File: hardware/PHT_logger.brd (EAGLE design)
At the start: 75 x 45 mm, 14 parts, among them IC3 ESP32-S3-WROOM-1-N16R2

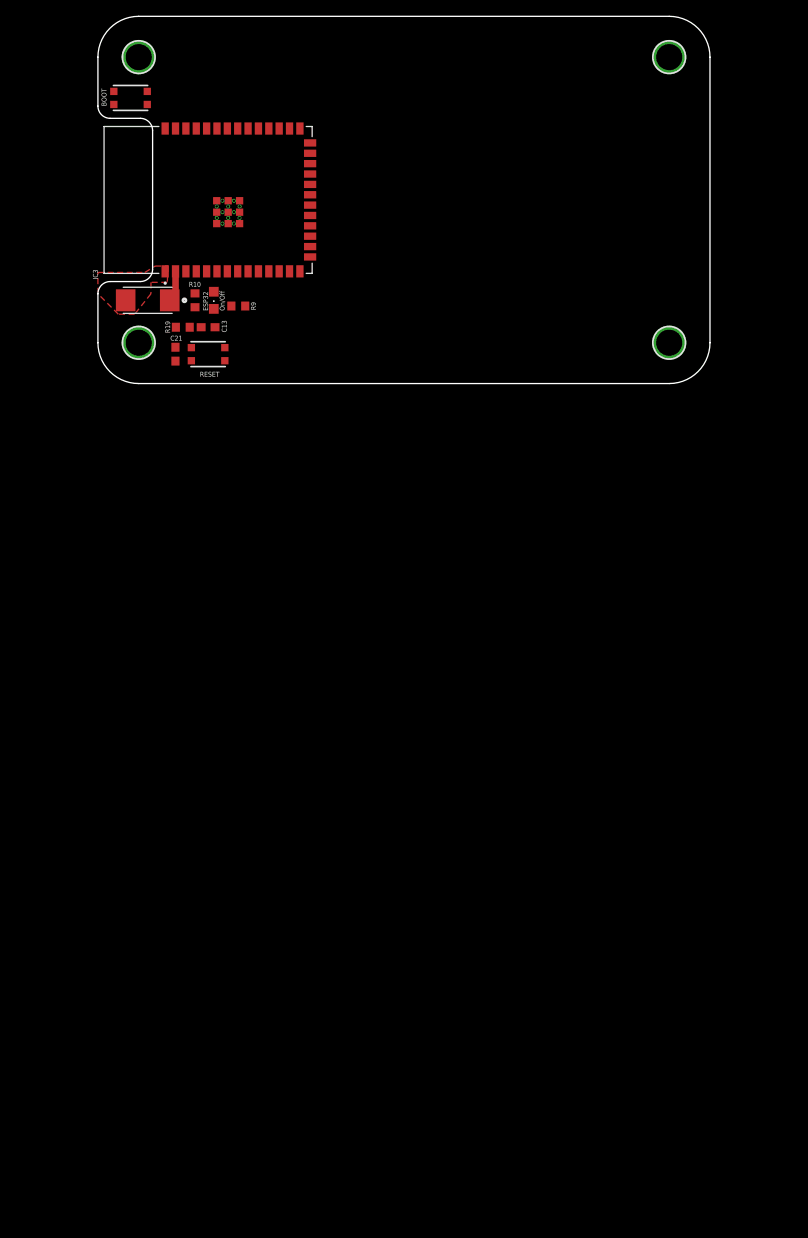
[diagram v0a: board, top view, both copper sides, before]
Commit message: Powe components updated on schematics
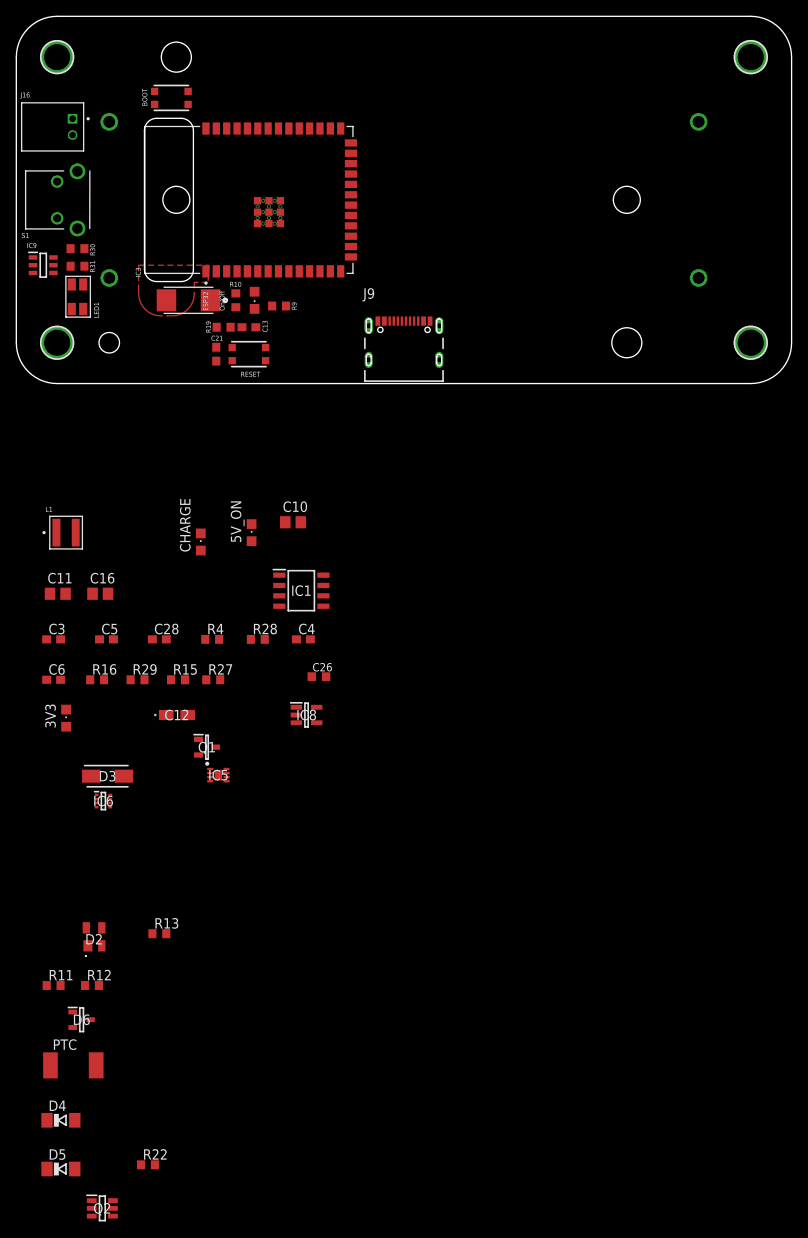
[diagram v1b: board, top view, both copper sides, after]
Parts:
- added 3V3: Red, led:CHIPLED_0805
- added 5V_ON: Yellow, led:CHIPLED_0805
- added BT1: 1049, 1049:BAT_1049
- added C10: 4.7uF, rcl:C0805
- added C11: 10uF, rcl:C0805
- added C12: T491A226M006AT7280, T491A226M006AT7280:T491A
- added C16: 22uF, rcl:C0805
- added C26: 10µF, rcl:C0603K
- added C28, C3, C5: 100nF, rcl:C0603
- added C4, C6: 10uF, rcl:C0603
- added CHARGE: Orange, led:CHIPLED_0805
- added D2: SP0503BAHTG, SP0503BAHTG:SP0503BAHTG
- added D3: RBR5L40ADDTE25, RBR5L40ADDTE25:DIOM5026X220N
- added D4, D5: bzv55-b5v6, diode:SOD80C
- added D6: BAT54,215, BAT54_215:SOT95P230X110-3N
- added IC1: AP2112M, AP2112M-3.3TRG1:SOIC127P600X170-8N
- added IC5: MAX17048G, MAX17048G+T10:SON50P200X200X80-9N
- added IC6: TPS610333DRLR, TPS610333DRLR:SOTFL50P160X60-8N
- added IC8: MCP73831T, MCP73831T-2ACI_OT:SOT95P270X145-5N
- added IC9: MAX16054AZT+T, MAX16054AZT+T:SOT95P275X110-6N
- added J16: S2B-PH, S2B-PH-K-S_LF__SN_:JST_S2B-PH-K-S(LF)(SN)
- added J9: USB4105-GF-A, USB4105-GF-A:GCT_USB4105-GF-A
- added L1: XFL4020-472MEC, XFL4020-472MEC:IND_XFL4020-472MEC
- added LED1: PWR_ON_OFF, OSRG1206C1C:3216(1206)-4
- added PTC: 1.5A, rcl:R2512
- added Q1: DMP2045U, DMP2045U-7:SOT96P240X110-3N
- added Q2: DMN2004DMK-7, DMN2004DMK-7:SOT95P285X145-6N
- added R11, R12: 5.1k, rcl:R0603
- added R13: 100k, rcl:R0603
- added R15, R22, R27, R30, R31: 1K, rcl:R0603
- added R16, R29: 5.1K, rcl:R0603
- added R28, R4: 100K, rcl:R0603
- added S1: 1-1825027-4, 1-1825027-4:118250274
- moved U$1 10.0 mm to (42.5, -17.5)
- moved U$2 10.0 mm to (-42.5, -17.5)
- moved U$3 10.0 mm to (-42.5, 17.5)
- moved U$4 10.0 mm to (42.5, 17.5)
- moved BOOT 5.00 mm to (-28.5, 12.5)
- moved C13 5.00 mm to (-19.0, -15.6)
- moved C15 5.00 mm to (-26.4, -12.3)
- moved C21 5.00 mm to (-23.0, -18.9)
- moved ESP32_ON 5.00 mm to (-18.3, -12.3)
- moved IC3 5.00 mm to (-19.0, 0.00)
- moved R10 5.00 mm to (-20.6, -12.3)
- moved R19 5.00 mm to (-22.1, -15.6)
- moved R9 5.00 mm to (-15.3, -13.0)
- moved RESET 5.00 mm to (-19.0, -18.9)
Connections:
- new net +5V: C11.2, C16.2, IC6.8, R15.1
- new net EXT_GND: D5.A, J9.S1, J9.S2, J9.S3, J9.S4, Q2.3, R13.2
- new net GATE_PROT: D4.A, Q2.5, R22.1
- new net LDO_EN: IC9.5, LED1.3, R28.1
- new net N$1: BT1.P2
- new net N$10: 5V_ON.A, R15.2
- new net N$11: CHARGE.C, R16.1
- new net N$12: IC9.4, LED1.1
- new net N$13: IC1.5, R28.2
- new net N$14: LED1.4, R30.2
- new net N$15: LED1.2, R31.2
- new net N$16: J9.B5, R11.2
- new net N$17: IC8.1, R16.2
- new net N$18: IC8.5, R29.2
- new net N$21: J9.A5, R12.2
- new net N$3: BT1.P1
- new net N$33: 3V3.A, R27.2
- new net N$9: IC6.7, L1.1
- new net PWR_BUTTON: IC9.1, S1.1
- new net USBBUS: D6.1, J9.A4_B9, J9.B4_A9
- new net USB_VBUS: D2.4, D6.3, PTC.1
- new net VBUS: CHARGE.A, D3.2, D4.C, D5.C, IC8.4, PTC.2, Q1.1, R22.2, R4.1
- new net VIN: C5.2, C6.2, D3.1, IC1.8, IC9.6, Q1.2, R30.1, R31.1
- new net V_BAT: C26.1, C28.1, IC5.2, IC5.3, IC8.3, J16.2, Q1.3
- net +3V3: now also C10.2, C12.1, C3.2, C4.2, IC1.1, IC6.1, IC6.5, L1.2, R27.1
- net 5V_ENABLE: now also IC6.2
- net BAT_ALERT: now also IC5.5
- net D+: now also D2.2, J9.A6, J9.B6
- net D-: now also D2.3, J9.A7, J9.B7
- net GND: now also 3V3.C, 5V_ON.C, BT1.N1, BT1.N2, C10.1, C11.1, C12.2, C16.1, C26.2, C28.2, C3.1, C4.1, C5.1, C6.1, D2.1, IC1.6, IC1.7, IC5.1, IC5.4, IC5.6, IC5.9, IC6.3, IC6.6, IC8.2, IC9.2, IC9.3, J16.1, J9.A1_B12, J9.B1_A12, Q2.4, R11.1, R12.1, R13.1, R29.1, R4.2, S1.2
- net SCL1: now also IC5.7
- net SDA1: now also IC5.8
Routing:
- net +3V3: track 3.84 -> 0.00 mm
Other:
- board size 75 x 45 mm -> 95 x 45 mm
